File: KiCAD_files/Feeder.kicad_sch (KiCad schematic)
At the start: 82 parts, among them J405 Conn_01x02_Male, J406 Conn_01x02_Male, J501 Conn_01x03, Q501 60V N channel, Q502 TK13P25D,RQ, T501 PA2467NL, U407 OPA316, U501 NCP12700, U503 TL431MFDT,215, U505 MCP1799T-5002H/DB

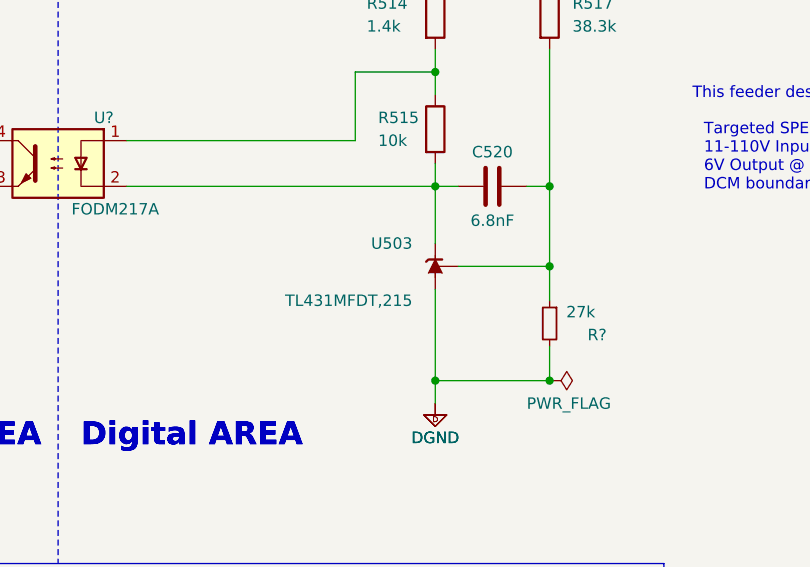
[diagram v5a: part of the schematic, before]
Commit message: forgot TL431 issue in previous commit, it is now taken into account
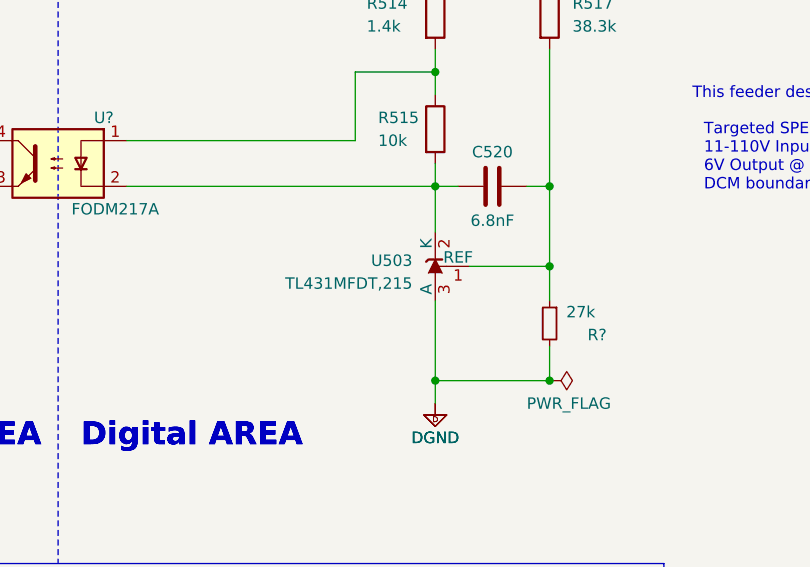
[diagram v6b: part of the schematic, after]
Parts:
- removed U503: TL431MFDT,215, Package_TO_SOT_SMD:SOT-23, symbol Reference_Voltage:TL431DBZ
- added U503: TL431MFDT,215, Package_TO_SOT_SMD:SOT-23, symbol Symbols:TL431MFDT
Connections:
- net DGND: now also U503.3 (A)
- net at C520.1, R515.2, U?.2: now also U503.2 (K)
- net at C520.2, R517.2, R?.1: now also U503.1 (REF)

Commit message: wip
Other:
- note added: "AZ1117CH : A minimum of 10uF capacitor (0.15Ω ≤ ESR ≤ 20Ω) must be connected from this pin to ground to insure stability"
- note removed: "VO : A minimum of 10uF capacitor (0.15Ω ≤ ESR ≤ 20Ω) must be connected from this pin to ground to insure stability"
- title: OWNVERTER V1.0 -> OWNVERTER V1.1
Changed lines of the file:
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@@
   (paper "A3")
   (title_block
-    (title "OWNVERTER V1.0")
+    (title "OWNVERTER V1.1")
     (comment 1 "TWR")
   )
@@
     (stroke (width 0.5) (type default))
   )
-  (polyline (pts (xy 231.14 15.24) (xy 231.14 218.44))
+  (polyline (pts (xy 231.14 12.7) (xy 231.14 218.44))
     (stroke (width 0.15) (type dash))
   )
@@
     (effects (font (size 1.27 1.27)) (justify left bottom))
   )
-  (text "VO : A minimum of 10uF\ncapacitor (0.15Ω ≤ ESR ≤ 20Ω) must\nbe connected from this pin\nto ground to insure stability"
-    (at 153.67 279.4 0)
+  (text "AZ1117CH : A minimum of 10uF\ncapacitor (0.15Ω ≤ ESR ≤ 20Ω) must\nbe connected from this pin\nto ground to insure stability"
+    (at 138.43 273.05 0)
     (effects (font (face "Arial") (size 1.27 1.27)) (justify left bottom))
   )
@@
   )
   (text "External power supply" (at 20.32 173.99 0)
-    (effects (font (size 2.4892 2.4892)) (justify left bottom))
+    (effects (font (size 2.54 2.54)) (justify left bottom))
   )
   (text "POWER AREA\n" (at 203.2 205.74 0)
@@
   )
   (text "+5V_DGND, +12V_PGND, +5V_PGND generation" (at 129.54 224.79 0)
-    (effects (font (face "Arial") (size 2.4892 2.4892) (thickness 0.4978) bold) (justify left bottom))
+    (effects (font (face "Arial") (size 2.54 2.54) (thickness 0.4978) bold) (justify left bottom))
   )
   (text "Type 2 Isolated feedback network with TL431\nAs per Application note DN05109-D\n\nExplanation\nhttps://www.onsemi.com/pub/Collateral/TND381-D.PDF\n\nR15 is the value to change the output voltage\nIt should be 27K to stabilize it to 6.05V\n\nTL431 give Vo = 6.05V\nwith Vo = VRef_DGND(1 + R14/R15)\n6.05V = 2,5V * (1 + 38,3K/27K)"

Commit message: correct datasheet link
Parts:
- C? (x4): manf# UMK212B7105KGHT -> UMK212B7105KGHT
- U407: manf# OPA316IDCKT -> MCP6487T-E/SN
